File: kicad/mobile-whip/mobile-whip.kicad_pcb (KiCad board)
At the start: 2 copper layers, 200 x 22 mm, 50 parts, among them J1 Conn_Coaxial, J2 USB_C_Receptacle_USB2.0, Q1 SI2301CDS-T1-GE3, Q2 SI2301CDS-T1-GE3, SW1 MK-12C02-G025, U1 LTC6268IS6, U2 TP4054, U3 LP2985-3.3, U4 TLV431

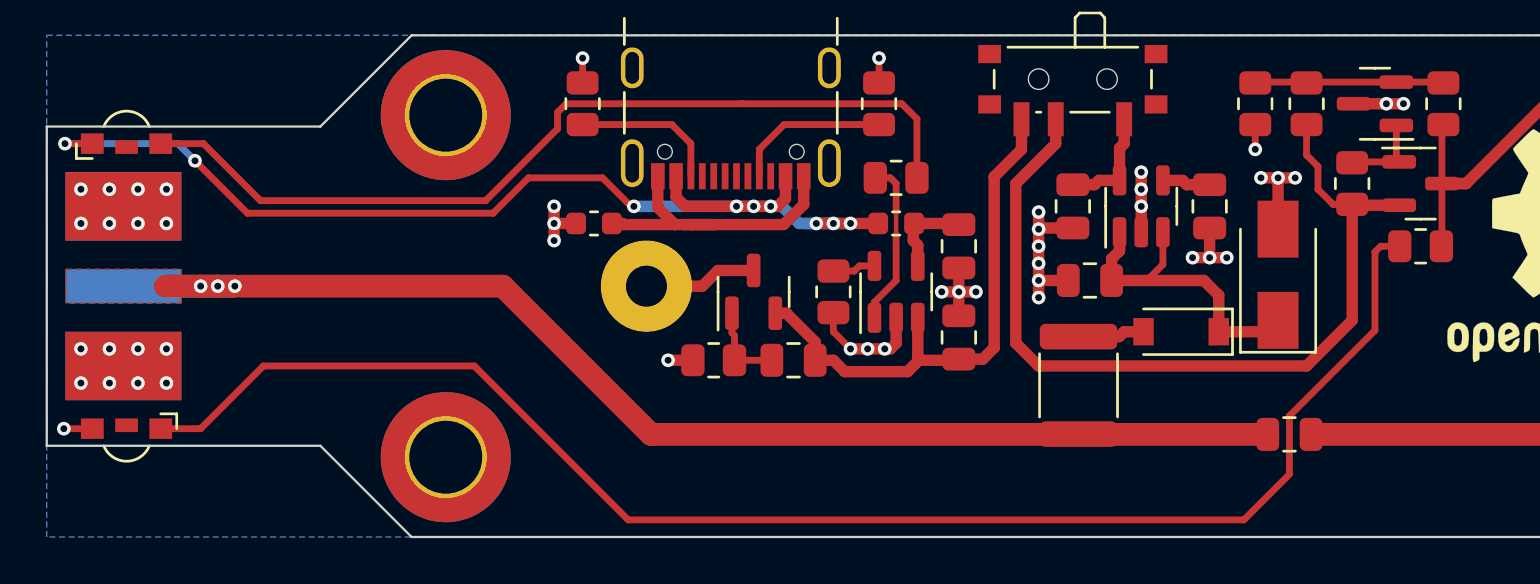
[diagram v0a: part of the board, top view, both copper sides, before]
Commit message: Fix LED footprint
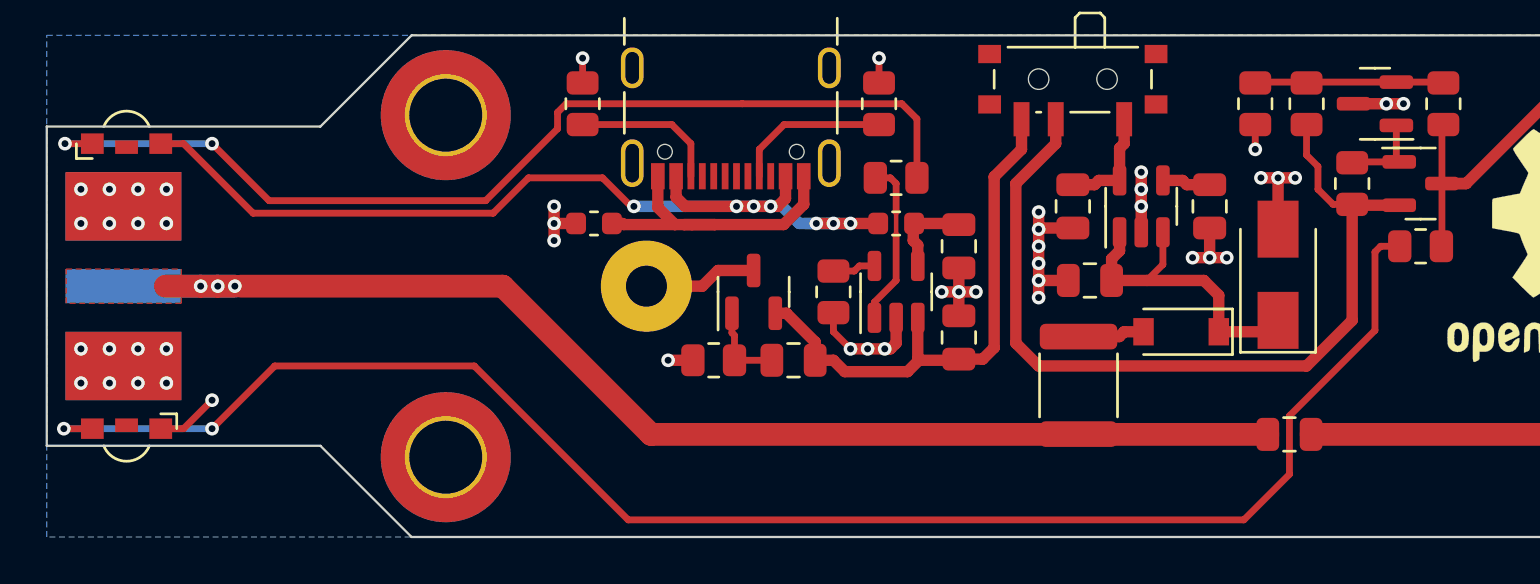
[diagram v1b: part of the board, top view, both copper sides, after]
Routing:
- net Net-(D1-Pad2): track 66.8 -> 72.3 mm, vias 0 -> 2
- net VBUS: track 49.3 -> 43.9 mm, vias 9 -> 7
- net Net-(D2-Pad1): track 39.5 -> 44.9 mm, vias 0 -> 2
- net GND: track 44.4 -> 45.9 mm

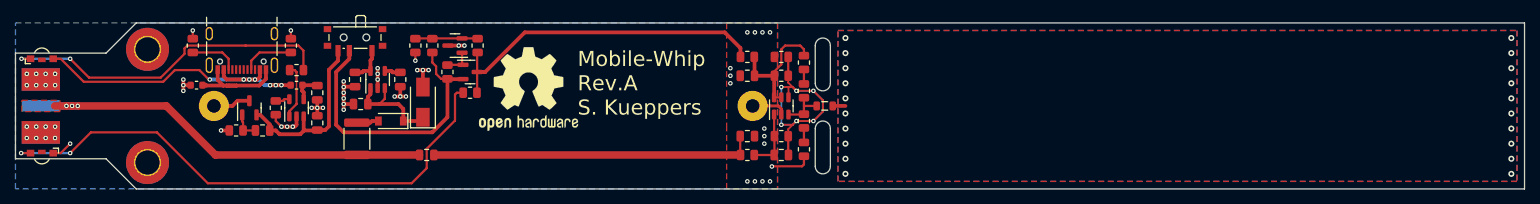
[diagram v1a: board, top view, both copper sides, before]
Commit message: Add tooling holes
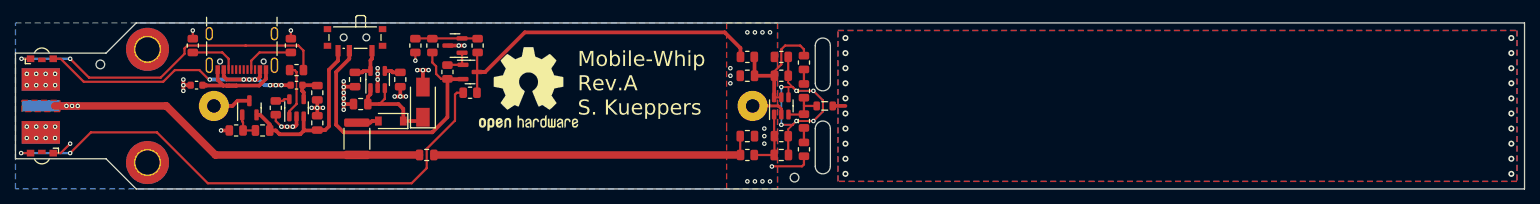
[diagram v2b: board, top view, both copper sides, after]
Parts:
- added H3: MountingHole, project:TOOLING-HOLE, F.Cu at (61.2, 74.5)
- added H4: MountingHole, project:TOOLING-HOLE, F.Cu at (153.2, 89.5)
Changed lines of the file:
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@@
     )
+  )
+  (footprint "project:TOOLING-HOLE" (layer "F.Cu")
+    (at 153.25 89.5)
+    (property "Sheetfile" "mobile-whip.kicad_sch")
+    (property "Sheetname" "")
+    (attr through_hole)
+    (fp_text reference "H4" (at -0.508 -2.54 unlocked) (layer "F.SilkS") hide
+      (effects (font (size 1 1) (thickness 0.15)))
+    )
+    (fp_text value "MountingHole" (at 0 3.048 unlocked) (layer "F.Fab") hide
+      (effects (font (size 1 1) (thickness 0.15)))
+    )
+    (fp_text user "${REFERENCE}" (at 0 4.572 unlocked) (layer "F.Fab") hide
+      (effects (font (size 1 1) (thickness 0.15)))
+    )
+    (pad "" np_thru_hole circle (at 0 0) (size 1.152 1.152) (drill 1.152) (layers F&B.Cu *.Mask)
+      (solder_mask_margin 0.15) (clearance 0.25))
   )
   (footprint "Symbol:OSHW-Logo2_14.6x12mm_SilkScreen" (layer "F.Cu")
@@
     )
   )
+  (footprint "project:TOOLING-HOLE" (layer "F.Cu")
+    (at 61.25 74.5)
+    (property "Sheetfile" "mobile-whip.kicad_sch")
+    (property "Sheetname" "")
+    (attr through_hole)
+    (fp_text reference "H3" (at -0.508 -2.54 unlocked) (layer "F.SilkS") hide
+      (effects (font (size 1 1) (thickness 0.15)))
+    )
+    (fp_text value "MountingHole" (at 0 3.048 unlocked) (layer "F.Fab") hide
+      (effects (font (size 1 1) (thickness 0.15)))
+    )
+    (fp_text user "${REFERENCE}" (at 0 4.572 unlocked) (layer "F.Fab") hide
+      (effects (font (size 1 1) (thickness 0.15)))
+    )
+    (pad "" np_thru_hole circle (at 0 0) (size 1.152 1.152) (drill 1.152) (layers F&B.Cu *.Mask)
+      (solder_mask_margin 0.15) (clearance 0.25))
+  )
   (footprint "project:SMA_Male_EdgeMount" (layer "B.Cu")

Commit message: Added component value to SMA connector
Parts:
- J1: value Conn_Coaxial -> SMA Edge Mount Male
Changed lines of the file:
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@@
     (property "Sheetfile" "mobile-whip.kicad_sch")
     (property "Sheetname" "")
-    (attr through_hole)
+    (attr through_hole exclude_from_pos_files)
     (fp_text reference "H4" (at -0.508 -2.54 unlocked) (layer "F.SilkS") hide
       (effects (font (size 1 1) (thickness 0.15)))
@@
     (property "Sheetfile" "mobile-whip.kicad_sch")
     (property "Sheetname" "")
-    (attr through_hole)
+    (attr through_hole exclude_from_pos_files)
     (fp_text reference "H3" (at -0.508 -2.54 unlocked) (layer "F.SilkS") hide
       (effects (font (size 1 1) (thickness 0.15)))
@@
       (effects (font (size 1 1) (thickness 0.15)) (justify mirror))
     )
-    (fp_text value "Conn_Coaxial" (at 5 -6) (layer "B.Fab") hide
+    (fp_text value "SMA Edge Mount Male" (at 5 -6) (layer "B.Fab") hide
       (effects (font (size 1 1) (thickness 0.15)) (justify mirror))
     )

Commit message: Use 100nF AC coupling cap
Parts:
- C5: value 10nF -> 100nF
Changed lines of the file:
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@@
       (effects (font (size 1 1) (thickness 0.15)))
     )
-    (fp_text value "10nF" (at 0 1.68) (layer "F.Fab") hide
+    (fp_text value "100nF" (at 0 1.68) (layer "F.Fab") hide
       (effects (font (size 1 1) (thickness 0.15)))
     )

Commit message: Changed some resistor values
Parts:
- R10: value 510R -> 220R
- R11: value 510R -> 470R
- R12, R5, R6: value 1K -> 2K
- R7: value 510R -> 1K
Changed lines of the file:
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@@
       (effects (font (size 1 1) (thickness 0.15)))
     )
-    (fp_text value "1K" (at 0 1.65) (layer "F.Fab") hide
+    (fp_text value "2K" (at 0 1.65) (layer "F.Fab") hide
       (effects (font (size 1 1) (thickness 0.15)))
     )
@@
       (effects (font (size 1 1) (thickness 0.15)))
     )
-    (fp_text value "510R" (at 0 1.65) (layer "F.Fab") hide
+    (fp_text value "1K" (at 0 1.65) (layer "F.Fab") hide
       (effects (font (size 1 1) (thickness 0.15)))
     )
@@
       (effects (font (size 1 1) (thickness 0.15)))
     )
-    (fp_text value "510R" (at 0 1.65) (layer "F.Fab") hide
+    (fp_text value "470R" (at 0 1.65) (layer "F.Fab") hide
       (effects (font (size 1 1) (thickness 0.15)))
     )
@@
       (effects (font (size 1 1) (thickness 0.15)))
     )
-    (fp_text value "1K" (at 0 1.65) (layer "F.Fab") hide
+    (fp_text value "2K" (at 0 1.65) (layer "F.Fab") hide
       (effects (font (size 1 1) (thickness 0.15)))
     )
@@
       (effects (font (size 1 1) (thickness 0.15)))
     )
-    (fp_text value "510R" (at 0 1.65) (layer "F.Fab") hide
+    (fp_text value "220R" (at 0 1.65) (layer "F.Fab") hide
       (effects (font (size 1 1) (thickness 0.15)))
     )
@@
       (effects (font (size 1 1) (thickness 0.15)))
     )
-    (fp_text value "1K" (at 0 1.65 90) (layer "F.Fab") hide
-      (effects (font (size 1 1) (thickness 0.15)))
-    )
+    (fp_text value "2K" (at 0 1.65 90) (layer "F.Fab") hide
+      (effects (font (size 1 1) (thickness 0.15)))
+    )

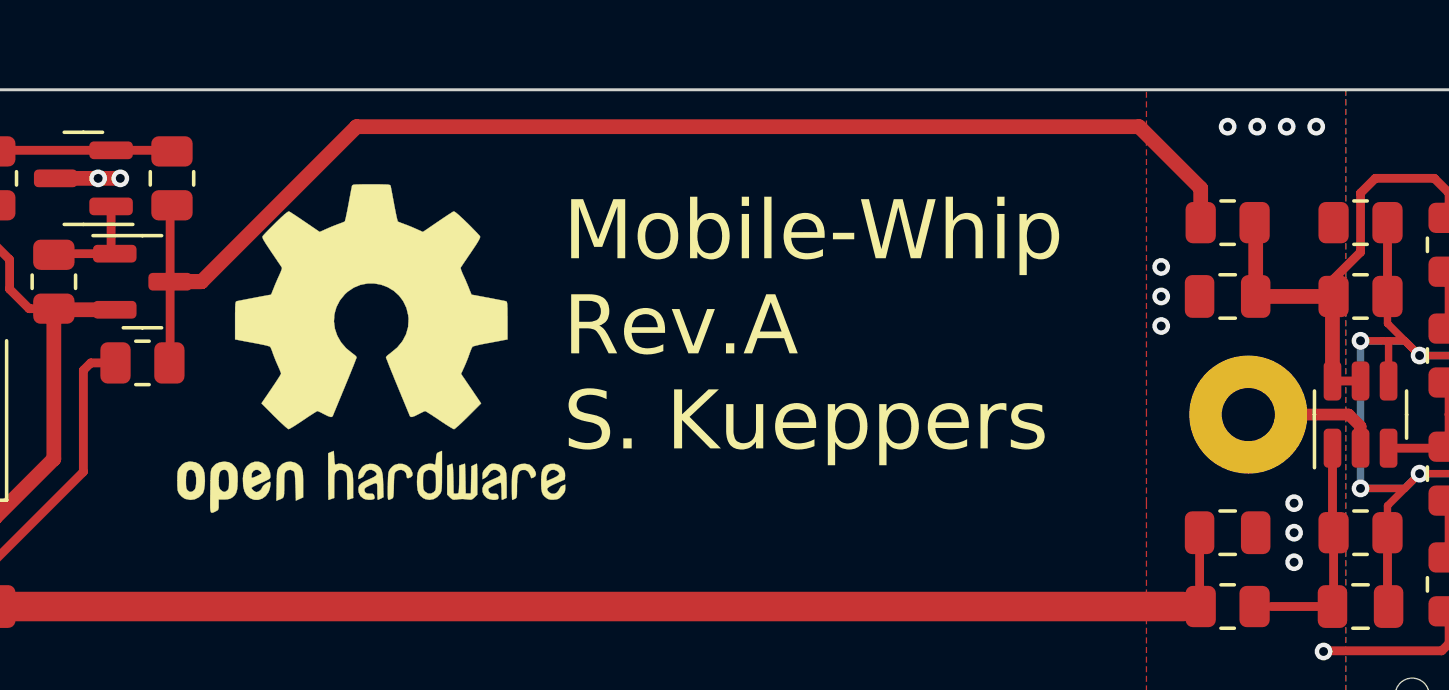
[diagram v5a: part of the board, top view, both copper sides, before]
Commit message: Choose OSHW symbol only
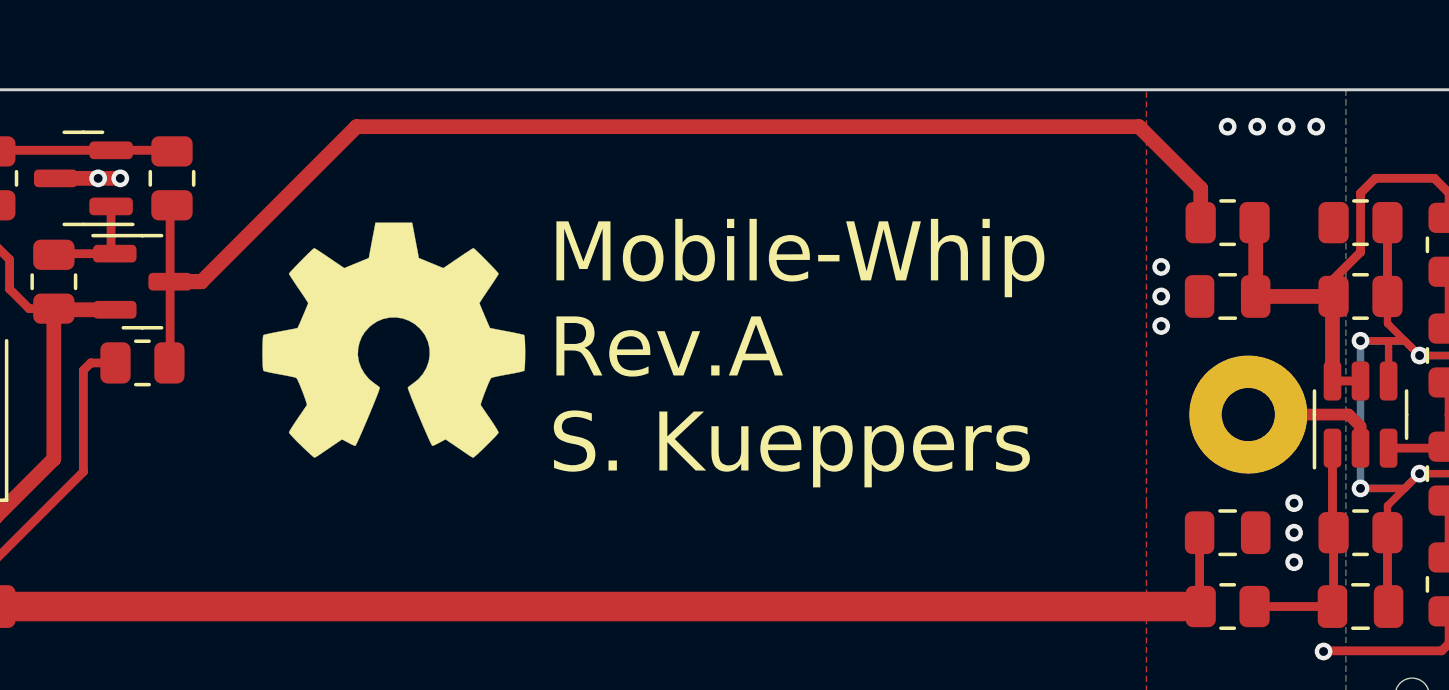
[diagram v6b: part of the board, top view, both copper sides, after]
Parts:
- removed the REF** at (118.0, 77.8)
- added REF**: OSHW-Symbol_8.9x8mm_SilkScreen, Symbol:OSHW-Symbol_8.9x8mm_SilkScreen, F.Cu at (118.8, 77.5)

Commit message: Final touches
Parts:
- added C11: 100nF, Capacitor_SMD:C_0805_2012Metric, F.Cu at (110.2, 81.0)
- added D4: B5819W SL, Diode_SMD:D_SOD-123, F.Cu at (111.5, 84.8)
- added D6: B5819W SL, Diode_SMD:D_SOD-123, F.Cu at (109.0, 84.8)
- moved C6 0.25 mm to (90.0, 78.0)
- moved C8 0.25 mm to (90.0, 82.5)
- moved FB1 0.25 mm to (87.2, 77.0)
- moved FB2 0.25 mm to (74.0, 77.0)
- moved R10 0.25 mm to (110.2, 78.5)
- moved R11 0.25 mm to (87.2, 75.0)
- moved R16 0.25 mm to (111.2, 71.8)
- moved R18 0.25 mm to (105.2, 71.8)
- moved R19 0.25 mm to (103.0, 71.8)
- moved U4 0.25 mm to (108.2, 71.8)
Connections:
- C9 pad 1: VDD -> Net-(C9-Pad1)
- Q1 pad 3: Net-(Q1-Pad3) -> VDD
- R1 pad 1: VDD -> Net-(C9-Pad1)
- R10 pad 2: Net-(Q1-Pad3) -> VDD
- R15 pad 1: VDD -> Net-(C9-Pad1)
- R15 pad 2: Net-(Q1-Pad3) -> VDD
- R16 pad 2: Net-(Q1-Pad3) -> VDD
- R5 pad 1: VDD -> Net-(C9-Pad1)
- U1 pad 5: VDD -> Net-(C9-Pad1)
- U1 pad 6: VDD -> Net-(C9-Pad1)
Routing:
- net Net-(Q1-Pad3): track 45.0 -> 0.00 mm
- net VDD: track 16.6 -> 48.7 mm
- net Net-(C9-Pad1): track 0.00 -> 16.6 mm
- net GND: track 45.9 -> 60.0 mm, vias 62 -> 70
- net Net-(R11-Pad1): track 7.30 -> 13.3 mm
- net +BATT: track 23.9 -> 24.7 mm
- net /ANT: vias 20 -> 18
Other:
- outline, holes or cut-outs redrawn

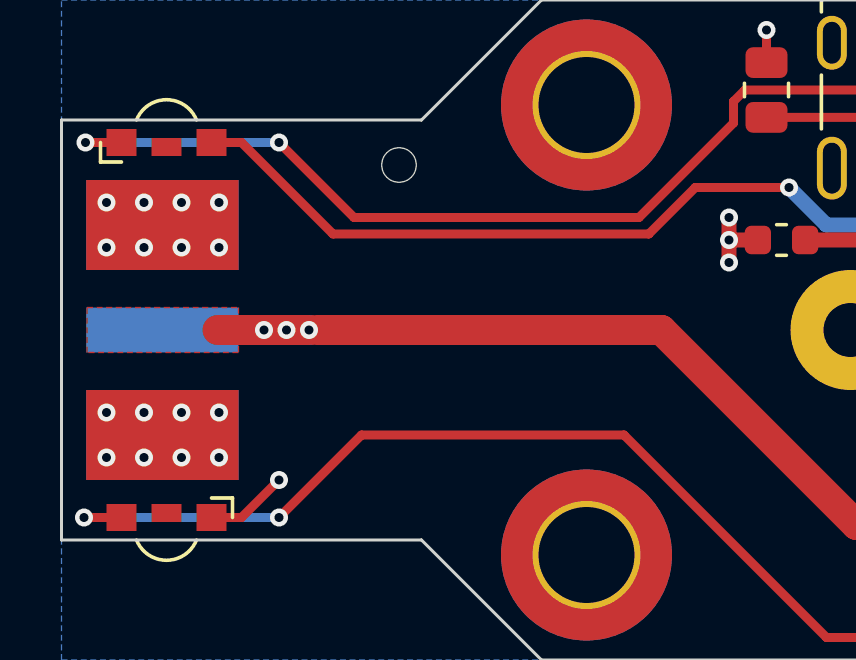
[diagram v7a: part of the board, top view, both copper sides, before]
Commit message: Move SMA edge mount further to the edge
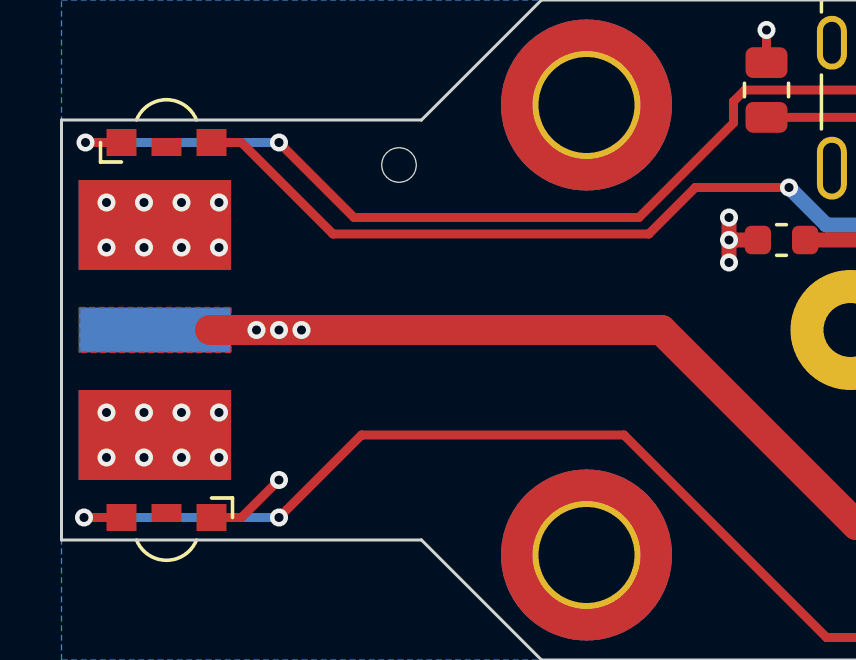
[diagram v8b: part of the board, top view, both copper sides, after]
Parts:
- moved J1 0.25 mm to (53.1, 80.0)
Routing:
- net /OUT: track 55.7 -> 56.2 mm
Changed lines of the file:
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@@
   )
   (footprint "project:SMA_Male_EdgeMount" (layer "B.Cu")
-    (at 53.3625 80 180)
+    (at 53.1125 80 180)
     (tags "SMA")
     (property "Sheetfile" "mobile-whip.kicad_sch")
@@
   (gr_circle (center 67.5 87.5) (end 71 87.5) (layer "B.Mask") (width 0) (fill solid))
   (gr_circle (center 67.5 72.5) (end 71 72.5) (layer "B.Mask") (width 0) (fill solid))
-  (gr_rect (start 50.85 79.25) (end 55.9 80.75) (layer "F.Mask") (width 0.15) (fill solid))
+  (gr_rect (start 50.6 79.25) (end 55.65 80.75) (layer "F.Mask") (width 0.15) (fill solid))
   (gr_arc (start 159.1 69) (mid 157.5 70.6) (end 155.9 69) (layer "Edge.Cuts") (width 0.1))
   (gr_line (start 155.9 69) (end 66 69) (layer "Edge.Cuts") (width 0.1))
@@
   (segment (start 113.0875 72.6625) (end 111.5 72.6625) (width 0.5) (layer "F.Cu") (net 25))
   (segment (start 111.1875 72.725) (end 111.25 72.6625) (width 0.3) (layer "F.Cu") (net 25))
+  (segment (start 58 80) (end 57.25 80) (width 1) (layer "F.Cu") (net 26))
+  (segment (start 70 80) (end 76.5 86.5) (width 1) (layer "F.Cu") (net 26))
+  (segment (start 58 80) (end 70 80) (width 1) (layer "F.Cu") (net 26))
+  (segment (start 56.5 80) (end 54.95 80) (width 1) (layer "F.Cu") (net 26))
+  (segment (start 57.25 80) (end 56.5 80) (width 1) (layer "F.Cu") (net 26))
   (segment (start 76.5 86.5) (end 103.55 86.5) (width 1) (layer "F.Cu") (net 26))
-  (segment (start 58.25 80) (end 57.5 80) (width 1) (layer "F.Cu") (net 26))
-  (segment (start 58.5 80) (end 70 80) (width 1) (layer "F.Cu") (net 26))
-  (segment (start 70 80) (end 76.5 86.5) (width 1) (layer "F.Cu") (net 26))
-  (segment (start 56.75 80) (end 55.2 80) (width 1) (layer "F.Cu") (net 26))
-  (segment (start 57.5 80) (end 56.75 80) (width 1) (layer "F.Cu") (net 26))
-  (via (at 58.25 80) (size 0.6) (drill 0.3) (layers "F.Cu" "B.Cu") (net 26))
-  (via (at 56.75 80) (size 0.6) (drill 0.3) (layers "F.Cu" "B.Cu") (net 26))
-  (via (at 57.5 80) (size 0.6) (drill 0.3) (layers "F.Cu" "B.Cu") (net 26))
-  (segment (start 58.25 80) (end 53.3625 80) (width 1) (layer "B.Cu") (net 26))
+  (via (at 58 80) (size 0.6) (drill 0.3) (layers "F.Cu" "B.Cu") (net 26))
+  (via (at 56.5 80) (size 0.6) (drill 0.3) (layers "F.Cu" "B.Cu") (net 26))
+  (via (at 57.25 80) (size 0.6) (drill 0.3) (layers "F.Cu" "B.Cu") (net 26))
+  (segment (start 58 80) (end 53.1125 80) (width 1) (layer "B.Cu") (net 26))
   (segment (start 77.6 75.18) (end 77.6 76.1) (width 0.5) (layer "F.Cu") (net 27))
   (segment (start 77.6 76.1) (end 78 76.5) (width 0.5) (layer "F.Cu") (net 27))
@@
     (polygon
       (pts
-        (xy 55.9 80.75)
-        (xy 50.85 80.75)
-        (xy 50.85 79.25)
-        (xy 55.9 79.25)
+        (xy 55.65 80.75)
+        (xy 50.6 80.75)
+        (xy 50.6 79.25)
+        (xy 55.65 79.25)
       )
     )
